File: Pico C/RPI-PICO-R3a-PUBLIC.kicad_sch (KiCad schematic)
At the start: 37 parts, among them IC1 W25Q16JVUXIQ, J1 CON_PICO_40W_VER_C, J2 USB_C_Receptacle_USB2.0_16P, J3 SM03B-SRSS-TB, Q1 DMG1012T-7, U2 RT6150B-33GQW, Y1 ECS-120-8-33-JGN-TR

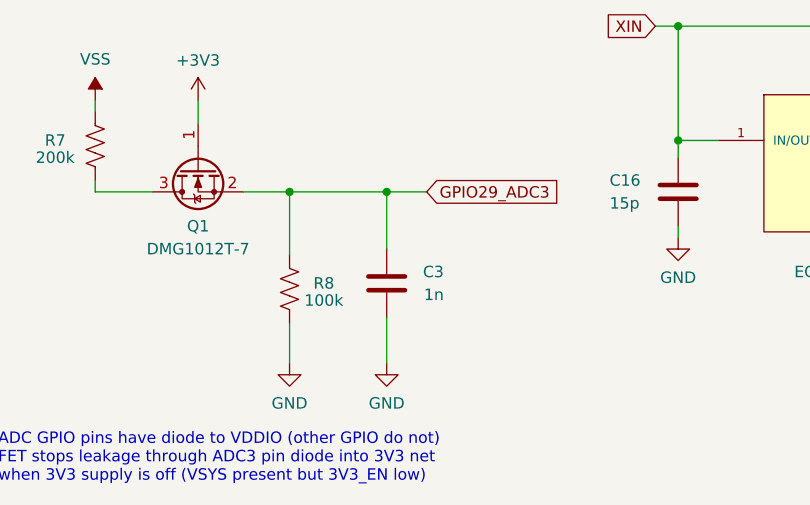
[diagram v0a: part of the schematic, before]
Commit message: Add files via upload
Upload boardview file for use with OpenBoardView.
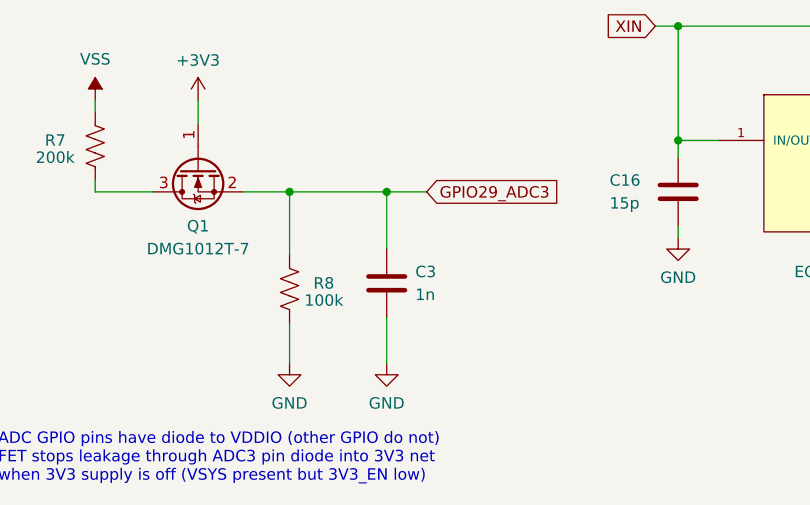
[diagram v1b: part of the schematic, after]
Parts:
- C15, C16, C17, C3: footprint Capacitor_SMD:C_0201_0603Metric -> Pico_C:C_0201_0603Metric
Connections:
- net GND: now also C3.2; no longer C3.1
- net GPIO29_ADC3: now also C3.1; no longer C3.2
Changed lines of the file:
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@@
       (effects (font (size 1.27 1.27)) (justify left))
     )
-    (property "Footprint" "Capacitor_SMD:C_0201_0603Metric" (at 186.3852 156.21 0)
+    (property "Footprint" "Pico_C:C_0201_0603Metric" (at 186.3852 156.21 0)
       (effects (font (size 1.27 1.27)) hide)
     )
@@
       (effects (font (size 1.27 1.27)) (justify left))
     )
-    (property "Footprint" "Capacitor_SMD:C_0201_0603Metric" (at 236.5502 155.575 0)
+    (property "Footprint" "Pico_C:C_0201_0603Metric" (at 236.5502 155.575 0)
       (effects (font (size 1.27 1.27)) hide)
     )
@@
         (path "/f8a1033e-7d4e-4018-9b4c-1da5b150b31c"
           (reference "#PWR046") (unit 1)
-        )
-      )
-    )
-  )
-  (symbol (lib_id "Device:C") (at 153.035 162.56 180) (unit 1)
-    (in_bom yes) (on_board yes) (dnp no)
-    (property "Reference" "C3" (at 159.385 161.29 0)
-      (effects (font (size 1.27 1.27)) (justify left))
-    )
-    (property "Value" "1n" (at 159.385 163.83 0)
-      (effects (font (size 1.27 1.27)) (justify left))
-    )
-    (property "Footprint" "Capacitor_SMD:C_0201_0603Metric" (at 152.0698 158.75 0)
-      (effects (font (size 1.27 1.27)) hide)
-    )
-    (property "Datasheet" "~" (at 153.035 162.56 0)
-      (effects (font (size 1.27 1.27)) hide)
-    )
-    (pin "1")
-    (pin "2")
-    (instances
-      (project "RPI-PICO-R3a-PUBLIC"
-        (path "/f8a1033e-7d4e-4018-9b4c-1da5b150b31c"
-          (reference "C3") (unit 1)
         )
       )
@@
         (path "/f8a1033e-7d4e-4018-9b4c-1da5b150b31c"
           (reference "R8") (unit 1)
+        )
+      )
+    )
+  )
+  (symbol (lib_id "Device:C") (at 153.035 162.56 0) (unit 1)
+    (in_bom yes) (on_board yes) (dnp no) (fields_autoplaced)
+    (property "Reference" "C3" (at 156.21 161.29 0)
+      (effects (font (size 1.27 1.27)) (justify left))
+    )
+    (property "Value" "1n" (at 156.21 163.83 0)
+      (effects (font (size 1.27 1.27)) (justify left))
+    )
+    (property "Footprint" "Pico_C:C_0201_0603Metric" (at 154.0002 166.37 0)
+      (effects (font (size 1.27 1.27)) hide)
+    )
+    (property "Datasheet" "~" (at 153.035 162.56 0)
+      (effects (font (size 1.27 1.27)) hide)
+    )
+    (pin "1")
+    (pin "2")
+    (instances
+      (project "RPI-PICO-R3a-PUBLIC"
+        (path "/f8a1033e-7d4e-4018-9b4c-1da5b150b31c"
+          (reference "C3") (unit 1)
         )
       )
@@
       (effects (font (size 1.27 1.27)) (justify left))
     )
-    (property "Footprint" "Capacitor_SMD:C_0201_0603Metric" (at 199.7202 118.745 0)
-      (effects (font (size 1.27 1.27)) hide)
-    )
+    (property "Footprint" "Pico_C:C_0201_0603Metric" (at 199.7202 118.745 0)
+      (effects (font (size 1.27 1.27)) hide)
+    )

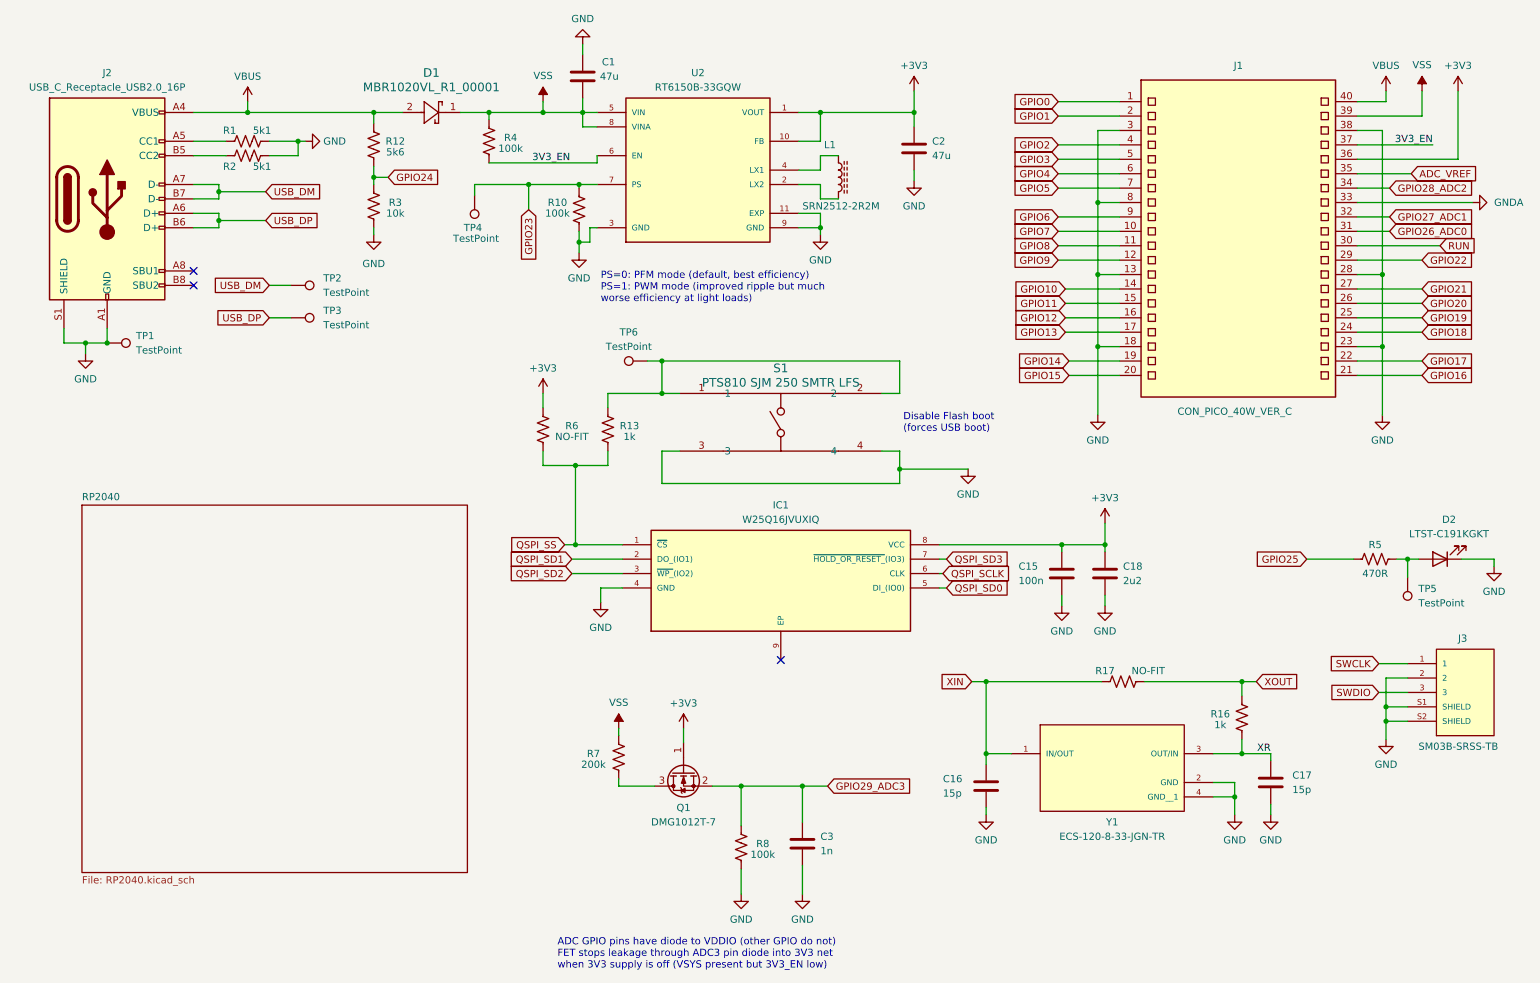
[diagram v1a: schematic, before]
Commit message: Add files via upload
Changed VSS to VS to reflect that it is a system voltage and not a negative supply/GND.
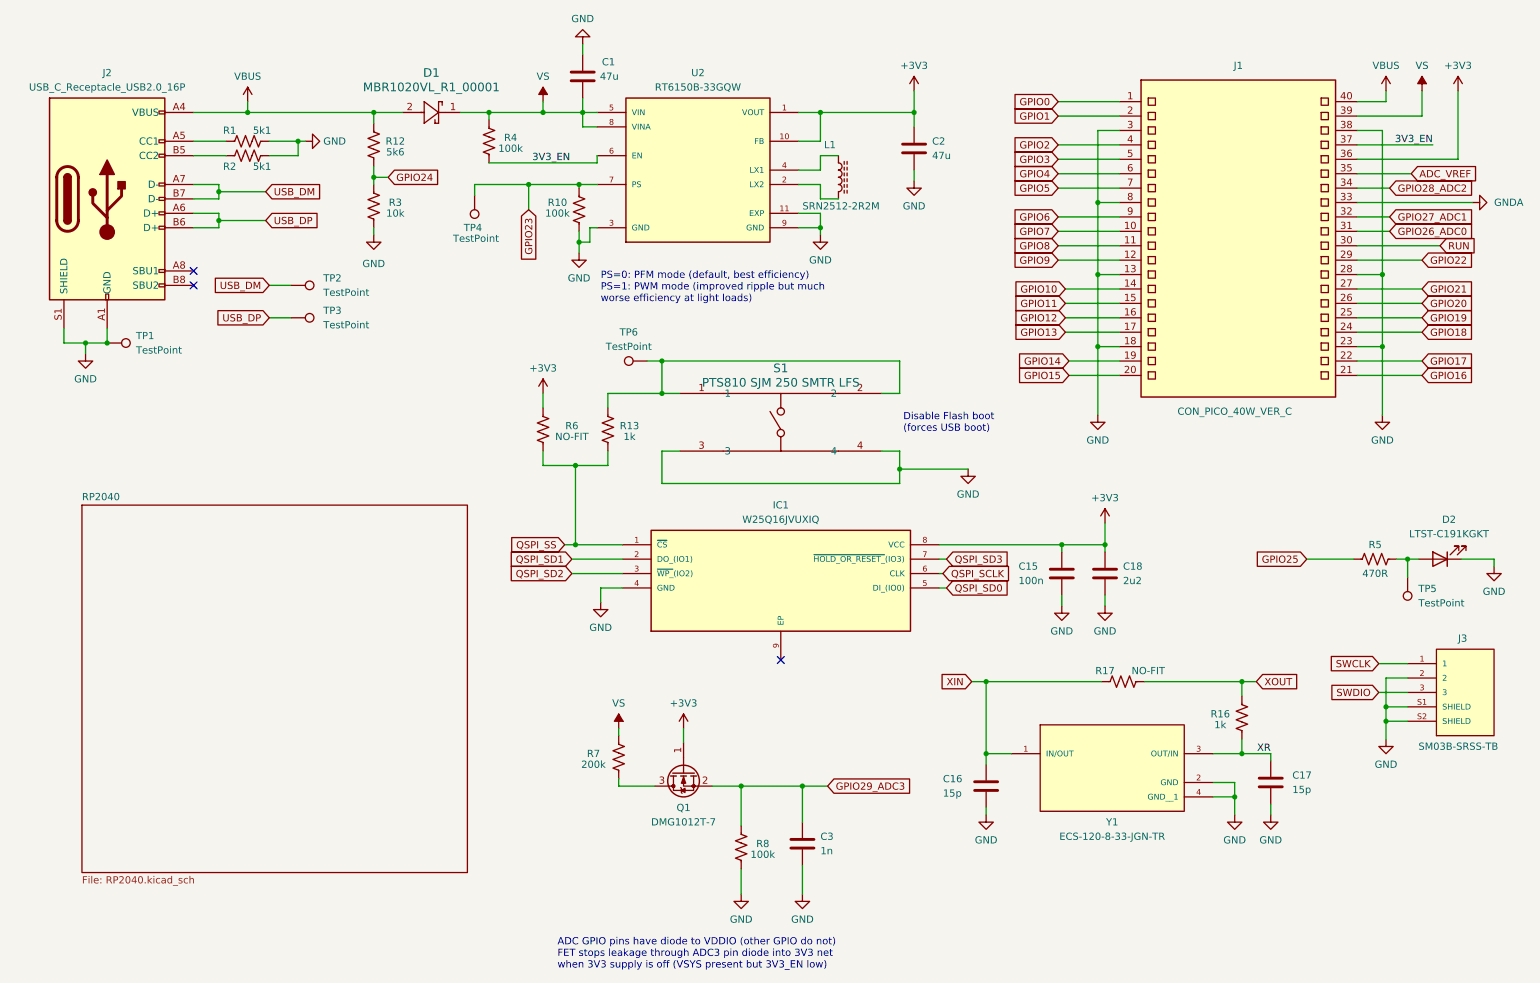
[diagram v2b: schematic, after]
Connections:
- net VSS renamed VS
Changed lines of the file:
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@@
-    )
-  )
-  (symbol (lib_id "power:VSS") (at 107.315 31.75 0) (unit 1)
-    (in_bom yes) (on_board yes) (dnp no) (fields_autoplaced)
-    (property "Reference" "#PWR09" (at 107.315 35.56 0)
-      (effects (font (size 1.27 1.27)) hide)
-    )
-    (property "Value" "VSS" (at 107.315 27.178 0)
-      (effects (font (size 1.27 1.27)))
-    )
-    (property "Footprint" "" (at 107.315 31.75 0)
-      (effects (font (size 1.27 1.27)) hide)
-    )
-    (property "Datasheet" "" (at 107.315 31.75 0)
-      (effects (font (size 1.27 1.27)) hide)
-    )
-    (pin "1")
-    (instances
-      (project "RPI-PICO-R3a-PUBLIC"
-        (path "/f8a1033e-7d4e-4018-9b4c-1da5b150b31c"
-          (reference "#PWR09") (unit 1)
-        )
-      )
     )
   )
@@
         (path "/f8a1033e-7d4e-4018-9b4c-1da5b150b31c"
           (reference "D1") (unit 1)
+        )
+      )
+    )
+  )
+  (symbol (lib_id "power:VS") (at 120.65 142.24 0) (unit 1)
+    (in_bom yes) (on_board yes) (dnp no) (fields_autoplaced)
+    (property "Reference" "#PWR024" (at 115.57 146.05 0)
+      (effects (font (size 1.27 1.27)) hide)
+    )
+    (property "Value" "VS" (at 120.65 137.795 0)
+      (effects (font (size 1.27 1.27)))
+    )
+    (property "Footprint" "" (at 120.65 142.24 0)
+      (effects (font (size 1.27 1.27)) hide)
+    )
+    (property "Datasheet" "" (at 120.65 142.24 0)
+      (effects (font (size 1.27 1.27)) hide)
+    )
+    (pin "1")
+    (instances
+      (project "RPI-PICO-R3a-PUBLIC"
+        (path "/f8a1033e-7d4e-4018-9b4c-1da5b150b31c"
+          (reference "#PWR024") (unit 1)
         )
       )
@@
     )
   )
-  (symbol (lib_id "power:VSS") (at 262.255 29.845 0) (unit 1)
-    (in_bom yes) (on_board yes) (dnp no) (fields_autoplaced)
-    (property "Reference" "#PWR024" (at 262.255 33.655 0)
-      (effects (font (size 1.27 1.27)) hide)
-    )
-    (property "Value" "VSS" (at 262.255 25.273 0)
-      (effects (font (size 1.27 1.27)))
-    )
-    (property "Footprint" "" (at 262.255 29.845 0)
-      (effects (font (size 1.27 1.27)) hide)
-    )
-    (property "Datasheet" "" (at 262.255 29.845 0)
-      (effects (font (size 1.27 1.27)) hide)
-    )
-    (pin "1")
-    (instances
-      (project "RPI-PICO-R3a-PUBLIC"
-        (path "/f8a1033e-7d4e-4018-9b4c-1da5b150b31c"
-          (reference "#PWR024") (unit 1)
-        )
-      )
-    )
-  )
   (symbol (lib_id "Device:C") (at 235.585 151.765 0) (unit 1)
     (in_bom yes) (on_board yes) (dnp no)
@@
     )
   )
+  (symbol (lib_id "power:VS") (at 107.315 31.75 0) (unit 1)
+    (in_bom yes) (on_board yes) (dnp no) (fields_autoplaced)
+    (property "Reference" "#PWR027" (at 102.235 35.56 0)
+      (effects (font (size 1.27 1.27)) hide)
+    )
+    (property "Value" "VS" (at 107.315 27.305 0)
+      (effects (font (size 1.27 1.27)))
+    )
+    (property "Footprint" "" (at 107.315 31.75 0)
+      (effects (font (size 1.27 1.27)) hide)
+    )
+    (property "Datasheet" "" (at 107.315 31.75 0)
+      (effects (font (size 1.27 1.27)) hide)
+    )
+    (pin "1")
+    (instances
+      (project "RPI-PICO-R3a-PUBLIC"
+        (path "/f8a1033e-7d4e-4018-9b4c-1da5b150b31c"
+          (reference "#PWR027") (unit 1)
+        )
+      )
+    )
+  )
   (symbol (lib_id "Device:R_US") (at 254 112.395 90) (unit 1)
     (in_bom yes) (on_board yes) (dnp no)
@@
         (path "/f8a1033e-7d4e-4018-9b4c-1da5b150b31c"
           (reference "#PWR022") (unit 1)
-        )
-      )
-    )
-  )
-  (symbol (lib_id "power:VSS") (at 120.65 142.24 0) (unit 1)
-    (in_bom yes) (on_board yes) (dnp no) (fields_autoplaced)
-    (property "Reference" "#PWR027" (at 120.65 146.05 0)
-      (effects (font (size 1.27 1.27)) hide)
-    )
-    (property "Value" "VSS" (at 120.65 137.668 0)
-      (effects (font (size 1.27 1.27)))
-    )
-    (property "Footprint" "" (at 120.65 142.24 0)
-      (effects (font (size 1.27 1.27)) hide)
-    )
-    (property "Datasheet" "" (at 120.65 142.24 0)
-      (effects (font (size 1.27 1.27)) hide)
-    )
-    (pin "1")
-    (instances
-      (project "RPI-PICO-R3a-PUBLIC"
-        (path "/f8a1033e-7d4e-4018-9b4c-1da5b150b31c"
-          (reference "#PWR027") (unit 1)
         )
       )
@@
         )
       )
+    )
+  )
+  (symbol (lib_id "power:VS") (at 262.255 29.845 0) (unit 1)
+    (in_bom yes) (on_board yes) (dnp no) (fields_autoplaced)
+    (property "Reference" "#PWR047" (at 257.175 33.655 0)
+      (effects (font (size 1.27 1.27)) hide)
+    )
+    (property "Value" "VS" (at 262.255 25.4 0)
+      (effects (font (size 1.27 1.27)))
+    )
+    (property "Footprint" "" (at 262.255 29.845 0)
+      (effects (font (size 1.27 1.27)) hide)
+    )
+    (property "Datasheet" "" (at 262.255 29.845 0)
+      (effects (font (size 1.27 1.27)) hide)
+    )
+    (pin "1")
+    (instances
+      (project "RPI-PICO-R3a-PUBLIC"
+        (path "/f8a1033e-7d4e-4018-9b4c-1da5b150b31c"
+          (reference "#PWR047") (unit 1)
+        )
+      )
